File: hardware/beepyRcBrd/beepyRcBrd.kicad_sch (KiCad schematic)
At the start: 4 parts, among them J19 Conn_01x05, J7 Conn_01x02

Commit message: fix: net names
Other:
- sheet IO ports: added ACC_INT; removed none
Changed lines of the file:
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@@
 	(wire
 		(pts
-			(xy 181.61 54.61) (xy 195.58 54.61)
+			(xy 181.61 60.96) (xy 195.58 60.96)
 		)
 		(stroke
@@
 	(wire
 		(pts
-			(xy 181.61 66.04) (xy 195.58 66.04)
+			(xy 181.61 71.12) (xy 195.58 71.12)
 		)
 		(stroke
@@
 	(wire
 		(pts
-			(xy 181.61 68.58) (xy 195.58 68.58)
+			(xy 181.61 73.66) (xy 195.58 73.66)
 		)
 		(stroke
@@
 	(wire
 		(pts
+			(xy 43.18 91.44) (xy 59.69 91.44)
+		)
+		(stroke
+			(width 0)
+			(type default)
+		)
+	)
+	(wire
+		(pts
 			(xy 168.91 138.43) (xy 168.91 152.4)
 		)
@@
 	(wire
 		(pts
-			(xy 181.61 57.15) (xy 195.58 57.15)
+			(xy 181.61 63.5) (xy 195.58 63.5)
 		)
 		(stroke
@@
 	(wire
 		(pts
-			(xy 181.61 59.69) (xy 195.58 59.69)
+			(xy 181.61 66.04) (xy 195.58 66.04)
 		)
 		(stroke
@@
 	(wire
 		(pts
+			(xy 181.61 52.07) (xy 195.58 52.07)
+		)
+		(stroke
+			(width 0)
+			(type default)
+		)
+	)
+	(wire
+		(pts
 			(xy 181.61 49.53) (xy 195.58 49.53)
 		)
@@
 		)
 	)
+	(label "M2_PWM_B"
+		(at 110.49 97.79 0)
+		(effects
+			(font
+				(size 1.27 1.27)
+			)
+			(justify left bottom)
+		)
+	)
 	(label "GNSS_PPS"
 		(at 43.18 81.28 0)
@@
 	)
 	(label "GNSS_TX"
-		(at 186.69 54.61 0)
+		(at 186.69 60.96 0)
 		(effects
 			(font
@@
 	)
 	(label "GNSS_RX"
-		(at 186.69 57.15 0)
+		(at 186.69 63.5 0)
 		(effects
 			(font
@@
 		)
 	)
-	(label "M2_ENC_B"
-		(at 217.17 54.61 0)
-		(effects
-			(font
-				(size 1.27 1.27)
-			)
-			(justify left bottom)
-		)
-	)
 	(label "SPI_MOSI"
 		(at 186.69 44.45 0)
@@
 	)
 	(label "GNSS_PPS"
-		(at 185.42 59.69 0)
+		(at 185.42 66.04 0)
 		(effects
 			(font
@@
 	)
 	(label "I2C_SCL"
-		(at 187.96 66.04 0)
+		(at 187.96 71.12 0)
 		(effects
 			(font
@@
 		)
 	)
-	(label "M2_ENC_B"
-		(at 110.49 97.79 0)
+	(label "ACC_INT"
+		(at 187.96 52.07 0)
 		(effects
 			(font
@@
 	)
 	(label "I2C_SDA"
-		(at 187.96 68.58 0)
+		(at 187.96 73.66 0)
+		(effects
+			(font
+				(size 1.27 1.27)
+			)
+			(justify left bottom)
+		)
+	)
+	(label "ACC_INT"
+		(at 43.18 91.44 0)
 		(effects
 			(font
@@
 		)
 	)
+	(label "M2_PWM_B"
+		(at 217.17 54.61 0)
+		(effects
+			(font
+				(size 1.27 1.27)
+			)
+			(justify left bottom)
+		)
+	)
 	(label "VTX_CS"
 		(at 43.18 86.36 0)
@@
 	(sheet
 		(at 149.86 36.83)
-		(size 31.75 34.29)
+		(size 31.75 39.37)
 		(exclude_from_sim no)
 		(in_bom yes)
@@
 		)
 		(property "Sheetfile" "io.kicad_sch"
-			(at 149.86 71.7046 0)
+			(at 149.86 76.7846 0)
 			(effects
 				(font
@@
 		)
 		(pin "GNSS_PPS" output
-			(at 181.61 59.69 0)
+			(at 181.61 66.04 0)
 			(effects
 				(font
@@
 		)
 		(pin "GNSS_RX" output
-			(at 181.61 57.15 0)
+			(at 181.61 63.5 0)
 			(effects
 				(font
@@
 		)
 		(pin "GNSS_TX" input
-			(at 181.61 54.61 0)
+			(at 181.61 60.96 0)
 			(effects
 				(font
@@
 		)
 		(pin "I2C_SDA" bidirectional
-			(at 181.61 68.58 0)
+			(at 181.61 73.66 0)
 			(effects
 				(font
@@
 		)
 		(pin "I2C_SCL" input
-			(at 181.61 66.04 0)
+			(at 181.61 71.12 0)
+			(effects
+				(font
+					(size 1.27 1.27)
+				)
+				(justify right)
+			)
+		)
+		(pin "ACC_INT" output
+			(at 181.61 52.07 0)
 			(effects
 				(font

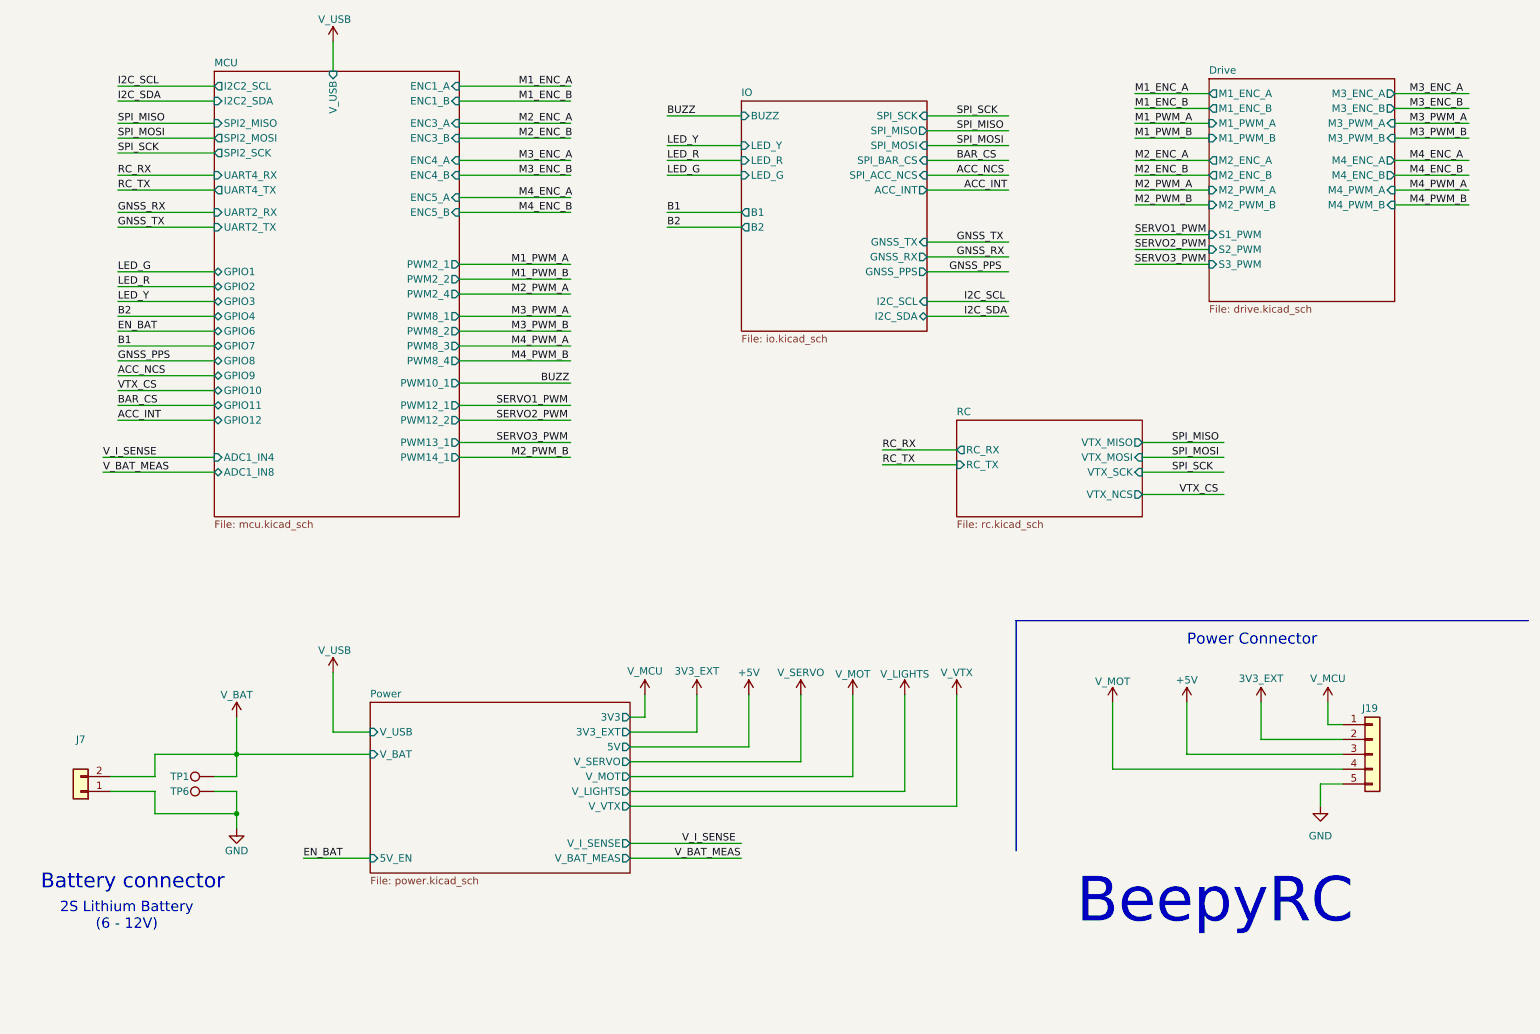
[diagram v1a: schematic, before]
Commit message: fix: passing schematics ERC rules
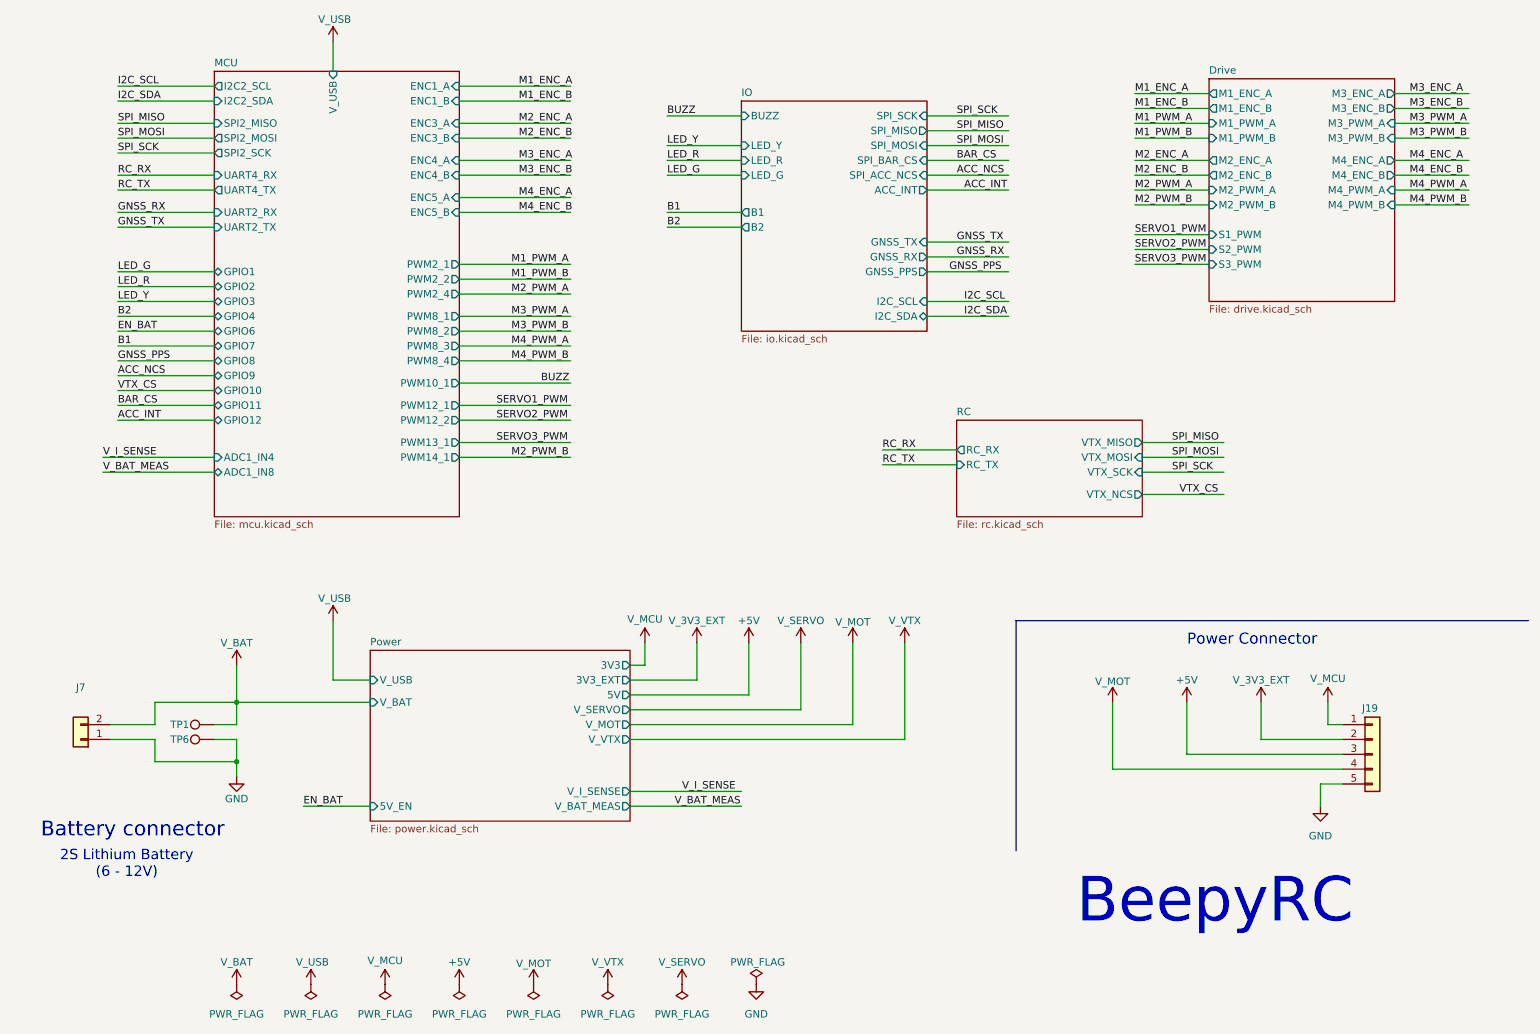
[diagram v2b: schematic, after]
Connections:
- net 3V3_EXT renamed V_3V3_EXT
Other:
- sheet Power ports: added none; removed V_LIGHTS
- moved on the sheet: J7, TP1, TP6

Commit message: feat: completed beepyRcBrd_rev_0_0.pdf
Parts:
- removed TP1, TP6: TestPoint, TestPoint:TestPoint_Pad_D2.5mm, symbol beepyRc_symbols:TestPoint
- added H1, H2, H3, H4: MT, beepyRcBrd:MountingHole_4.3mm_M4_DIN965_Pad_TopBottom, symbol beepyRc_symbols:MountingHole_Pad
- J19: footprint lscs:CONN-TH_5P-P3.50_DORABO_DB125-3.5-5P-GN-S -> beepyRcBrd:CONN-TH_5P-P3.50_DORABO_DB125-3.5-5P-GN-S
- J7: footprint lscs:CONN-TH_P5.00_KF301-5.0-2P -> beepyRcBrd:CONN-TH_P5.00_KF301-5.0-2P
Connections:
- net GND: now also H1.1, H2.1, H3.1, H4.1
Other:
- sheet IO ports: added V_USB; removed none
- sheet MCU ports: added none; removed V_USB
- note added: "Board Mounting Holes"
